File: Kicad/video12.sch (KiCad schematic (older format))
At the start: 18 parts, among them J1201 DE15HD, U1201 THS7316, U1202 TPD7S019

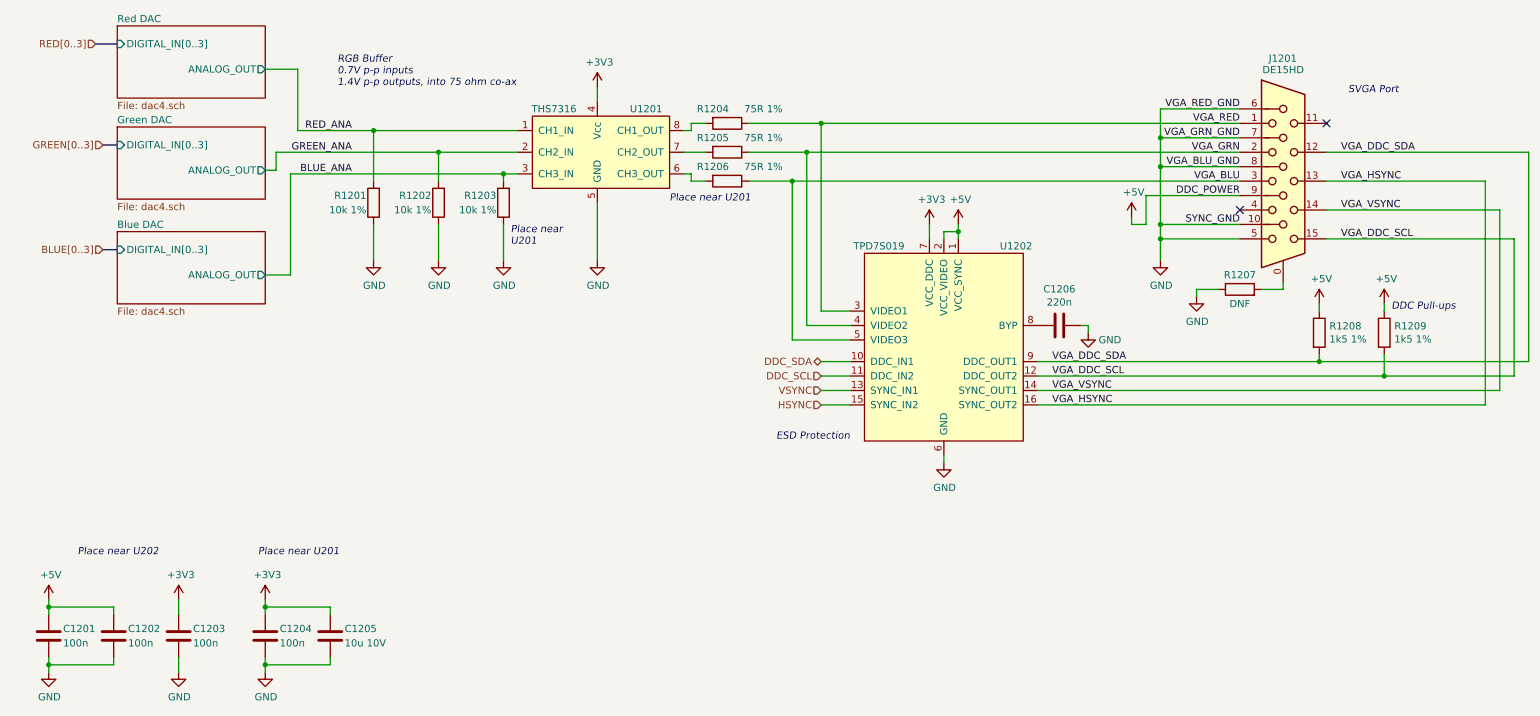
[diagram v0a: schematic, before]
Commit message: Brought in sheets from Neotron Pico.
Also includes DB15HD and PSU 3D models.
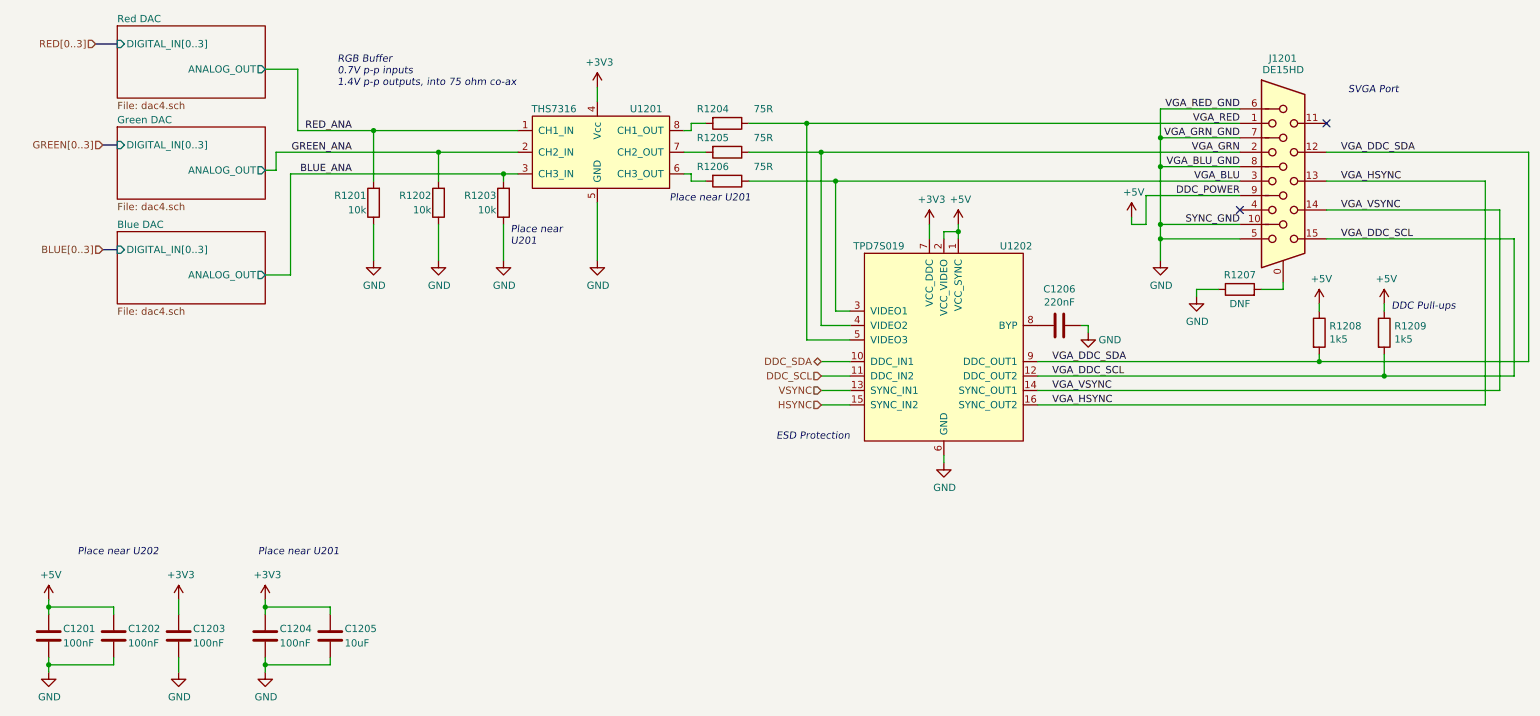
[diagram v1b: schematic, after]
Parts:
- C1201, C1202, C1203, C1204: value 100n -> 100nF; Digikey BC1150CT-ND -> (none); LCSC Part# (none) -> C49678; MPN K104K15X7RF5TL2 -> CPL-CAP-X7R-0805-100NF-50V; Manufacturer Vishay -> CPL; Mouser 594-K104K15X7RF5TL2 -> (none)
- C1205: value 10u 10V -> 10uF; Digikey 1276-6455-1-ND -> (none); LCSC Part# (none) -> C15850; MPN CL21A106KOQNNNG -> CPL-CAP-X5R-0805-10UF-16V; Manufacturer Samsung -> CPL
- C1206: value 220n -> 220nF; LCSC Part# (none) -> C5378
- J1201: footprint Connector_Dsub:DSUB-15-HD_Female_Horizontal_P2.29x1.98mm_EdgePinOffset3.03mm_Housed_MountingHolesOffset4.94mm -> Neotron-Common-Hardware:Amphenol_ICD15S13E4GV00LF
- R1201, R1202, R1203: value 10k 1% -> 10k; Digikey RMCF0805FT10K0-ND -> (none); LCSC Part# (none) -> C17414; MPN RMCF0805FT10K0 -> CPL-RES-0805-10K-0.125W; Manufacturer Stackpole -> CPL
- R1204, R1205, R1206: value 75R 1% -> 75R; LCSC Part# (none) -> C20638
- R1208, R1209: value 1k5 1% -> 1k5; LCSC Part# (none) -> C4310
- U1201: LCSC Part# (none) -> C155446
- U1202: LCSC Part# (none) -> C337499
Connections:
- net VGA_BLU: now also U1202.3 (VIDEO1); no longer U1202.5 (VIDEO3)
- net VGA_RED: now also U1202.5 (VIDEO3); no longer U1202.3 (VIDEO1)

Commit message: Merge in more changes.
Mostly lowering voltage tolerances to minimum required.
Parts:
- C1201, C1202: Tolerance (none) -> X5R; Voltage (none) -> 16V
- C1203, C1204, C1205: Tolerance (none) -> X5R; Voltage (none) -> 10V
- C1206: Tolerance (none) -> X5R; Voltage (none) -> 50V
- J1201: footprint Neotron-Common-Hardware:Amphenol_ICD15S13E4GV00LF -> neotron-pico:Amphenol_ICD15S13E4GV00LF
- R1201, R1202, R1203, R1204, R1205, R1206, R1208, R1209: Tolerance (none) -> 1%
- U1201: MPN THS7316 -> THS7316DR
- U1202: MPN TPD7S019 -> TPD7S019-15DBQR
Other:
- note added: "Place near THS7316"
- note added: "Place near\nTHS7316"
- note added: "TPD7S019"
- note removed: "Place near U201"
- note removed: "Place near U202"
- note removed: "Place near\nU201"
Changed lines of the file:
@@
 $Descr A4 11693 8268
 encoding utf-8
-Sheet 12 18
-Title "Neotron Common Hardware"
-Date "2021-06-18"
+Sheet 4 18
+Title ""
+Date "2021-06-10"
 Rev "[Uncontrolled]"
 Comp "https://neotron-compute.github.io/"
@@
 F 0 "J1201" H 9250 4850 50  0000 L CNN
 F 1 "DE15HD" H 9350 4800 50  0000 C TNN
-F 2 "Neotron-Common-Hardware:Amphenol_ICD15S13E4GV00LF" H 8400 4400 50  0001 C CNN
+F 2 "neotron-pico:Amphenol_ICD15S13E4GV00LF" H 8400 4400 50  0001 C CNN
 F 3 "~" H 8400 4400 50  0001 C CNN
 F 4 "0" H 9350 4000 50  0001 C CNN "DNP"
@@
 F 8 "649-ICD15S13E4GV00LF" H 9350 4000 50  0001 C CNN "Mouser"
 F 9 "~" H 9350 4000 50  0001 C CNN "LCSC Part#"
+F 10 "~" H 9350 4000 50  0001 C CNN "Tolerance"
+F 11 "~" H 9350 4000 50  0001 C CNN "Voltage"
 	1    9350 4000
 	1    0    0    -1
@@
 F 7 "Stackpole" H 5500 3600 50  0001 C CNN "Manufacturer"
 F 8 "C20638" H 5500 3600 50  0001 C CNN "LCSC Part#"
+F 9 "1%" H 5500 3600 50  0001 C CNN "Tolerance"
+F 10 "~" H 5500 3600 50  0001 C CNN "Voltage"
 	1    5500 3600
 	0    1    1    0
@@
 F 7 "Stackpole" H 5500 3800 50  0001 C CNN "Manufacturer"
 F 8 "C20638" H 5500 3800 50  0001 C CNN "LCSC Part#"
+F 9 "1%" H 5500 3800 50  0001 C CNN "Tolerance"
+F 10 "~" H 5500 3800 50  0001 C CNN "Voltage"
 	1    5500 3800
 	0    1    1    0
@@
 F 7 "Stackpole" H 5500 4000 50  0001 C CNN "Manufacturer"
 F 8 "C20638" H 5500 4000 50  0001 C CNN "LCSC Part#"
+F 9 "1%" H 5500 4000 50  0001 C CNN "Tolerance"
+F 10 "~" H 5500 4000 50  0001 C CNN "Voltage"
 	1    5500 4000
 	0    1    1    0
@@
 F 3 "~" H 3050 4150 50  0001 C CNN
 F 4 "0" H 3050 4150 50  0001 C CNN "DNP"
-F 5 "" H 3050 4150 50  0001 C CNN "Digikey"
+F 5 "~" H 3050 4150 50  0001 C CNN "Digikey"
 F 6 "CPL-RES-0805-10K-0.125W" H 3050 4150 50  0001 C CNN "MPN"
 F 7 "CPL" H 3050 4150 50  0001 C CNN "Manufacturer"
 F 8 "C17414" H 3050 4150 50  0001 C CNN "LCSC Part#"
+F 9 "1%" H 3050 4150 50  0001 C CNN "Tolerance"
+F 10 "~" H 3050 4150 50  0001 C CNN "Mouser"
+F 11 "~" H 3050 4150 50  0001 C CNN "Voltage"
 	1    3050 4150
 	-1   0    0    1
@@
 F 3 "~" H 3500 4150 50  0001 C CNN
 F 4 "0" H 3500 4150 50  0001 C CNN "DNP"
-F 5 "" H 3500 4150 50  0001 C CNN "Digikey"
+F 5 "~" H 3500 4150 50  0001 C CNN "Digikey"
 F 6 "CPL-RES-0805-10K-0.125W" H 3500 4150 50  0001 C CNN "MPN"
 F 7 "CPL" H 3500 4150 50  0001 C CNN "Manufacturer"
 F 8 "C17414" H 3500 4150 50  0001 C CNN "LCSC Part#"
+F 9 "1%" H 3500 4150 50  0001 C CNN "Tolerance"
+F 10 "~" H 3500 4150 50  0001 C CNN "Mouser"
+F 11 "~" H 3500 4150 50  0001 C CNN "Voltage"
 	1    3500 4150
 	-1   0    0    1
@@
 F 3 "~" H 3950 4150 50  0001 C CNN
 F 4 "0" H 3950 4150 50  0001 C CNN "DNP"
-F 5 "" H 3950 4150 50  0001 C CNN "Digikey"
+F 5 "~" H 3950 4150 50  0001 C CNN "Digikey"
 F 6 "CPL-RES-0805-10K-0.125W" H 3950 4150 50  0001 C CNN "MPN"
 F 7 "CPL" H 3950 4150 50  0001 C CNN "Manufacturer"
 F 8 "C17414" H 3950 4150 50  0001 C CNN "LCSC Part#"
+F 9 "1%" H 3950 4150 50  0001 C CNN "Tolerance"
+F 10 "~" H 3950 4150 50  0001 C CNN "Mouser"
+F 11 "~" H 3950 4150 50  0001 C CNN "Voltage"
 	1    3950 4150
 	-1   0    0    1
@@
 F 3 "https://www.ti.com/lit/ds/symlink/tpd7s019.pdf" H 7550 5200 50  0001 C CNN
 F 4 "Texas Instruments" H 7000 3750 50  0001 C CNN "Manufacturer"
-F 5 "TPD7S019" H 7000 3650 50  0001 C CNN "MPN"
+F 5 "TPD7S019-15DBQR" H 7000 3650 50  0001 C CNN "MPN"
 F 6 "0" H 7000 5100 50  0001 C CNN "DNP"
 F 7 "296-27595-1-ND" H 7000 5100 50  0001 C CNN "Digikey"
 F 8 "595-TPD7S019-15DBQR" H 7000 5100 50  0001 C CNN "Mouser"
 F 9 "C337499" H 7000 5100 50  0001 C CNN "LCSC Part#"
+F 10 "~" H 7000 5100 50  0001 C CNN "Tolerance"
+F 11 "~" H 7000 5100 50  0001 C CNN "Voltage"
 	1    7000 5100
 	1    0    0    -1
@@
 F 5 "0" H 4750 3800 50  0001 C CNN "DNP"
 F 6 "296-26684-1-ND" H 4750 3800 50  0001 C CNN "Digikey"
-F 7 "THS7316" H 4750 3800 50  0001 C CNN "MPN"
+F 7 "THS7316DR" H 4750 3800 50  0001 C CNN "MPN"
 F 8 "595-THS7316DR" H 4750 3800 50  0001 C CNN "Mouser"
 F 9 "C155446" H 4750 3800 50  0001 C CNN "LCSC Part#"
+F 10 "~" H 4750 3800 50  0001 C CNN "Tolerance"
+F 11 "~" H 4750 3800 50  0001 C CNN "Voltage"
 	1    4750 3800
 	1    0    0    -1
@@
 F 7 "Stackpole" H 9600 5050 50  0001 C CNN "Manufacturer"
 F 8 "C4310" H 9600 5050 50  0001 C CNN "LCSC Part#"
+F 9 "1%" H 9600 5050 50  0001 C CNN "Tolerance"
+F 10 "~" H 9600 5050 50  0001 C CNN "Voltage"
 	1    9600 5050
 	1    0    0    -1
@@
 F 7 "Stackpole" H 10050 5050 50  0001 C CNN "Manufacturer"
 F 8 "C4310" H 10050 5050 50  0001 C CNN "LCSC Part#"
+F 9 "1%" H 10050 5050 50  0001 C CNN "Tolerance"
+F 10 "~" H 10050 5050 50  0001 C CNN "Voltage"
 	1    10050 5050
 	1    0    0    -1
@@
 F 7 "Samsung" H 7800 5000 50  0001 C CNN "Manufacturer"
 F 8 "C5378" H 7800 5000 50  0001 C CNN "LCSC Part#"
+F 9 "X5R" H 7800 5000 50  0001 C CNN "Tolerance"
+F 10 "50V" H 7800 5000 50  0001 C CNN "Voltage"
+F 11 "~" H 7800 5000 50  0001 C CNN "Mouser"
 	1    7800 5000
 	0    1    1    0
@@
 F 3 "~" H 800 7150 50  0001 C CNN
 F 4 "0" H 800 7150 50  0001 C CNN "DNP"
-F 5 "" H 800 7150 50  0001 C CNN "Digikey"
+F 5 "~" H 800 7150 50  0001 C CNN "Digikey"
 F 6 "CPL-CAP-X7R-0805-100NF-50V" H 800 7150 50  0001 C CNN "MPN"
 F 7 "CPL" H 800 7150 50  0001 C CNN "Manufacturer"
-F 8 "" H 800 7150 50  0001 C CNN "Mouser"
+F 8 "~" H 800 7150 50  0001 C CNN "Mouser"
 F 9 "C49678" H 800 7150 50  0001 C CNN "LCSC Part#"
+F 10 "X5R" H 800 7150 50  0001 C CNN "Tolerance"
+F 11 "16V" H 800 7150 50  0001 C CNN "Voltage"
 	1    800  7150
 	-1   0    0    1
@@
 F 3 "~" H 1250 7150 50  0001 C CNN
 F 4 "0" H 1250 7150 50  0001 C CNN "DNP"
-F 5 "" H 1250 7150 50  0001 C CNN "Digikey"
+F 5 "~" H 1250 7150 50  0001 C CNN "Digikey"
 F 6 "CPL-CAP-X7R-0805-100NF-50V" H 1250 7150 50  0001 C CNN "MPN"
 F 7 "CPL" H 1250 7150 50  0001 C CNN "Manufacturer"
-F 8 "" H 1250 7150 50  0001 C CNN "Mouser"
+F 8 "~" H 1250 7150 50  0001 C CNN "Mouser"
 F 9 "C49678" H 1250 7150 50  0001 C CNN "LCSC Part#"
+F 10 "X5R" H 1250 7150 50  0001 C CNN "Tolerance"
+F 11 "16V" H 1250 7150 50  0001 C CNN "Voltage"
 	1    1250 7150
 	-1   0    0    1
@@
 $EndComp
 Text Notes 1000 6600 0    50   Italic 0
-Place near U202
+TPD7S019
 Text Notes 2250 6600 0    50   Italic 0
-Place near U201
+Place near THS7316
 $Comp
 L power:+3V3 #PWR01205
@@
 F 3 "~" H 2300 7150 50  0001 C CNN
 F 4 "0" H 2300 7150 50  0001 C CNN "DNP"
-F 5 "" H 2300 7150 50  0001 C CNN "Digikey"
+F 5 "~" H 2300 7150 50  0001 C CNN "Digikey"
 F 6 "CPL-CAP-X7R-0805-100NF-50V" H 2300 7150 50  0001 C CNN "MPN"
 F 7 "CPL" H 2300 7150 50  0001 C CNN "Manufacturer"
-F 8 "" H 2300 7150 50  0001 C CNN "Mouser"
+F 8 "~" H 2300 7150 50  0001 C CNN "Mouser"
 F 9 "C49678" H 2300 7150 50  0001 C CNN "LCSC Part#"
+F 10 "X5R" H 2300 7150 50  0001 C CNN "Tolerance"
+F 11 "10V" H 2300 7150 50  0001 C CNN "Voltage"
 	1    2300 7150
 	-1   0    0    1
@@
 F 3 "~" H 2750 7150 50  0001 C CNN
 F 4 "0" H 2750 7150 50  0001 C CNN "DNP"
-F 5 "" H 2750 7150 50  0001 C CNN "Digikey"
+F 5 "~" H 2750 7150 50  0001 C CNN "Digikey"
 F 6 "CPL-CAP-X5R-0805-10UF-16V" H 2750 7150 50  0001 C CNN "MPN"
 F 7 "CPL" H 2750 7150 50  0001 C CNN "Manufacturer"
 F 8 "C15850" H 2750 7150 50  0001 C CNN "LCSC Part#"
+F 9 "X5R" H 2750 7150 50  0001 C CNN "Tolerance"
+F 10 "10V" H 2750 7150 50  0001 C CNN "Voltage"
+F 11 "~" H 2750 7150 50  0001 C CNN "Mouser"
 	1    2750 7150
 	-1   0    0    -1
@@
 F 6 "~" H 9050 4750 50  0001 C CNN "MPN"
 F 7 "~" H 9050 4750 50  0001 C CNN "Manufacturer"
-F 8 "" H 9050 4750 50  0001 C CNN "Mouser"
+F 8 "~" H 9050 4750 50  0001 C CNN "Mouser"
 F 9 "~" H 9050 4750 50  0001 C CNN "LCSC Part#"
+F 10 "~" H 9050 4750 50  0001 C CNN "Tolerance"
+F 11 "~" H 9050 4750 50  0001 C CNN "Voltage"
 	1    9050 4750
 	0    -1   -1   0
@@
 Wire Wire Line
 	8000 5000 8000 5050
-Text Notes 5100 4150 0    50   Italic 0
-Place near U201
+Text Notes 5325 4250 0    50   Italic 0
+Place near\nTHS7316
 Text Notes 4000 4450 0    50   Italic 0
-Place near\nU201
+Place near\nTHS7316
 Text Label 2900 3650 2    50   ~ 0
 RED_ANA
@@
 F 3 "~" H 1700 7150 50  0001 C CNN
 F 4 "0" H 1700 7150 50  0001 C CNN "DNP"
-F 5 "" H 1700 7150 50  0001 C CNN "Digikey"
+F 5 "~" H 1700 7150 50  0001 C CNN "Digikey"
 F 6 "CPL-CAP-X7R-0805-100NF-50V" H 1700 7150 50  0001 C CNN "MPN"
 F 7 "CPL" H 1700 7150 50  0001 C CNN "Manufacturer"
-F 8 "" H 1700 7150 50  0001 C CNN "Mouser"
+F 8 "~" H 1700 7150 50  0001 C CNN "Mouser"
 F 9 "C49678" H 1700 7150 50  0001 C CNN "LCSC Part#"
+F 10 "X5R" H 1700 7150 50  0001 C CNN "Tolerance"
+F 11 "10V" H 1700 7150 50  0001 C CNN "Voltage"
 	1    1700 7150
 	-1   0    0    1

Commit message: Fixups after last copy-over.
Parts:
- J1201: footprint neotron-pico:Amphenol_ICD15S13E4GV00LF -> Neotron-Common-Hardware:Amphenol_ICD15S13E4GV00LF
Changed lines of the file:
@@
 F 0 "J1201" H 9250 4850 50  0000 L CNN
 F 1 "DE15HD" H 9350 4800 50  0000 C TNN
-F 2 "neotron-pico:Amphenol_ICD15S13E4GV00LF" H 8400 4400 50  0001 C CNN
+F 2 "Neotron-Common-Hardware:Amphenol_ICD15S13E4GV00LF" H 8400 4400 50  0001 C CNN
 F 3 "~" H 8400 4400 50  0001 C CNN
 F 4 "0" H 9350 4000 50  0001 C CNN "DNP"
